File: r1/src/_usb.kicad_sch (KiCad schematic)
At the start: 14 parts, among them J2 USB-C-12, J3 USB-A-10mm-flangeless, U3 CP2102N-A01-GQFN24

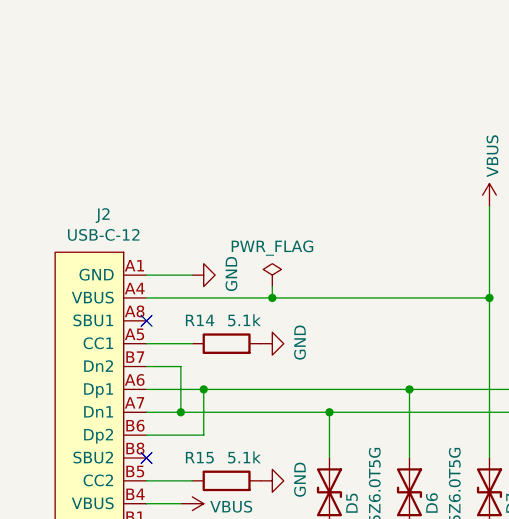
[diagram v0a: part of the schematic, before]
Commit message: Fix USB-C connector BoM data
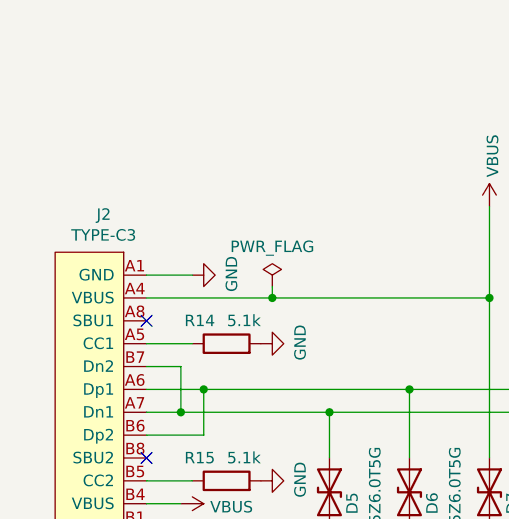
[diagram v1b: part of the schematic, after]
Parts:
- J2: value USB-C-12 -> TYPE-C3; LCSC C283540 -> C167321; MPN TYPE-C-31-M-17 -> 918-418K2023S40001; Manufacturer HRO -> Jing
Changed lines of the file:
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@@
       (effects (font (size 1.27 1.27)))
     )
-    (property "Value" "USB-C-12" (at 70.1802 59.0804 0)
+    (property "Value" "TYPE-C3" (at 70.1802 59.0804 0)
       (effects (font (size 1.27 1.27)))
     )
@@
       (effects (font (size 1.27 1.27)) hide)
     )
-    (property "MPN" "TYPE-C-31-M-17" (at 69.85 59.69 0)
+    (property "MPN" "918-418K2023S40001" (at 69.85 59.69 0)
       (effects (font (size 1.27 1.27)) hide)
     )
-    (property "LCSC" "C283540" (at 69.85 59.69 0)
+    (property "LCSC" "C167321" (at 69.85 59.69 0)
       (effects (font (size 1.27 1.27)) hide)
     )
-    (property "Manufacturer" "HRO" (at 69.85 59.69 0)
+    (property "Manufacturer" "Jing" (at 69.85 59.69 0)
       (effects (font (size 1.27 1.27)) hide)
     )
